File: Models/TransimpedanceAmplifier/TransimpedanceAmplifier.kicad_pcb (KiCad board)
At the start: 2 copper layers, 107 parts, among them J1 Conn_01x02_Socket, J10 Conn_01x02_Pin, J11 Conn_01x24_Socket, J14 Conn_01x24_Socket, J2 Conn_01x02_Socket, J3 Conn_01x03_Pin, J4 Conn_01x02_Pin, J5 Conn_01x02_Pin, J6 Conn_01x02_Pin, J7 Conn_01x02_Pin, J8 Conn_01x02_Pin, J9 Conn_01x02_Pin, Q1 Q_PNP, Q2 Q_NPN, U1 LM7905, -5V, 5%, U10 DAC81401, U11 ISO7641FM, U12 ISO7641FM, U13 ADS8699, U2 LM7805, 5V, 5%, U3 OPA828, U4 AD8615, U5 OP37GPZ, U6 LM7915, -15V, 5%, U7 LM7815, 15V, 5%, U8 LM7805, 5V, 5%, U9 TLV76133, 3.3V, 1%

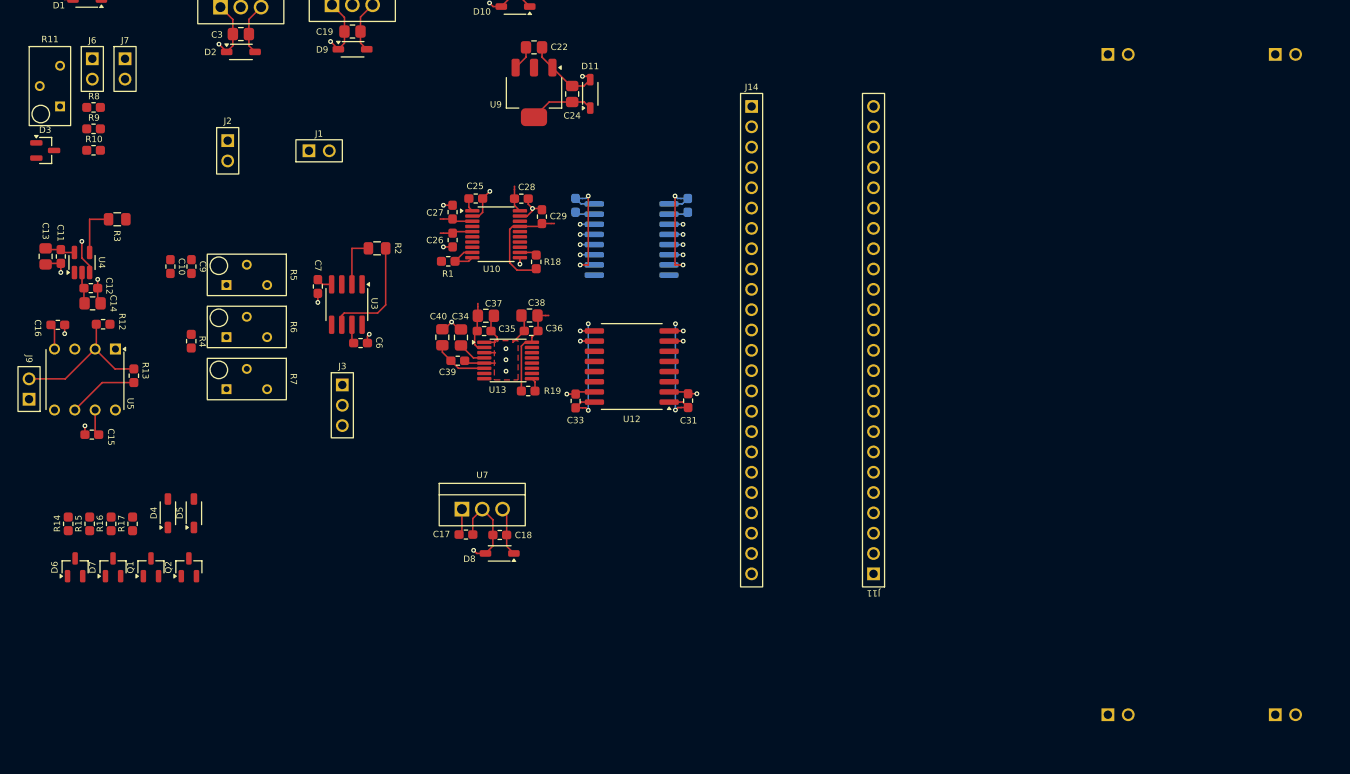
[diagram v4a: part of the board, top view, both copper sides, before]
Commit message: Added notes for power wiring
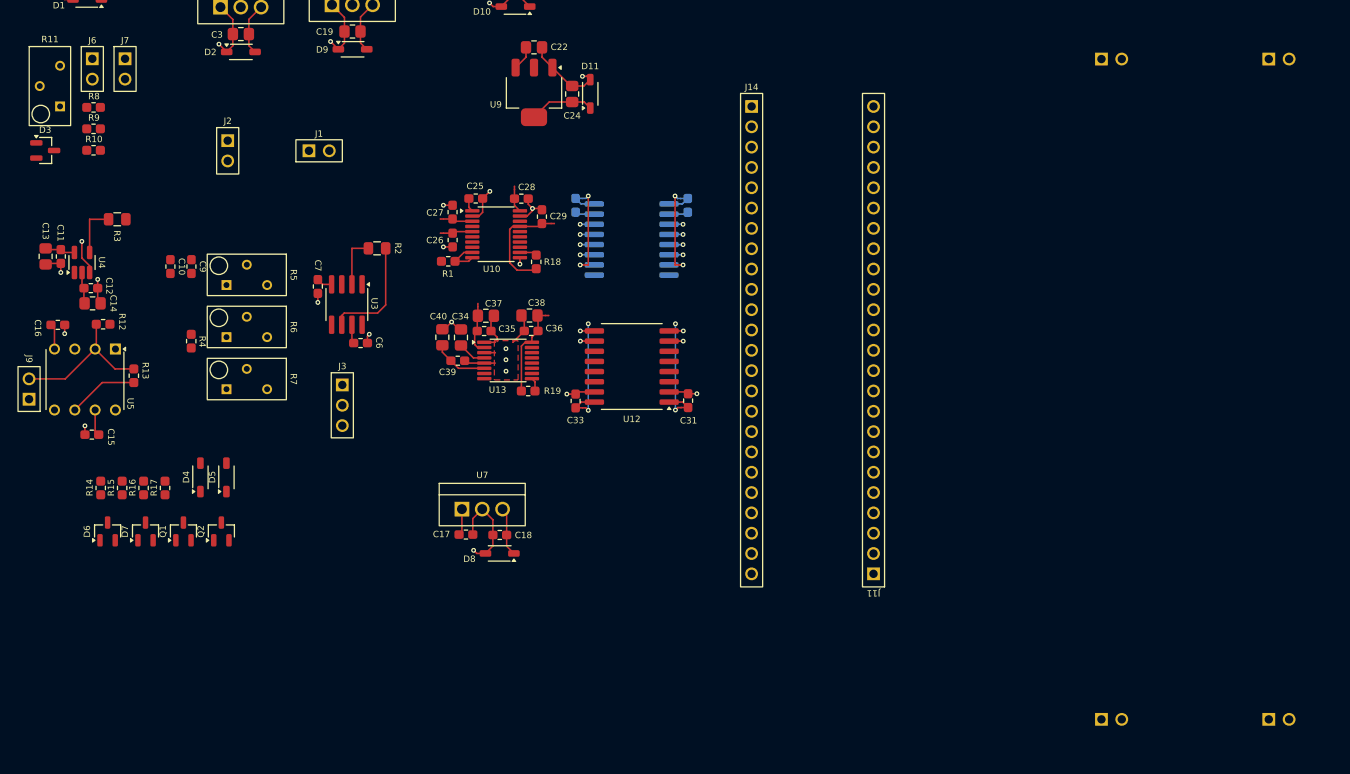
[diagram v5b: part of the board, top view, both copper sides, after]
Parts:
- moved R14 6.05 mm to (87.2, 125.0)
- moved R15 6.05 mm to (89.9, 125.0)
- moved R16 6.05 mm to (92.6, 125.0)
- moved R17 6.05 mm to (95.3, 125.0)
- moved D4 6.05 mm to (99.7, 123.7)
- moved D5 6.05 mm to (102.9, 123.7)
- moved D6 6.05 mm to (88.1, 130.5)
- moved Q1 6.05 mm to (97.6, 130.5)
- moved Q2 6.05 mm to (102.3, 130.5)
- moved D7 6.05 mm to (92.8, 130.5)
- moved BT1 1.00 mm to (224.0, 112.7)
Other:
- board text added: "-1.5 V"
- board text added: "-15 V"
- board text added: "-27 V"
- board text added: "-5 V"
- board text added: "15 V"
- board text added: "18 V"
- board text added: "2.5 V"
- board text added: "27 V"
- board text added: "3.3 V"
- board text added: "5 V"
- board text added: "Bring -15 V all the way around from top of board with long trace on left edge. Topology-wise, from left to right: Conductor connecting two battery terminals -15 V trace (transporting power to bottom) 15 V trace (transporting power to top) Either ordering of -15 V vs. 15 V has an unsavory crossover. Choose the best one after more relevant information is known."
- board text added: "Keep -1.5 V on top of board, route the colliding signal trace under it with vias. This is a much more workable option."
- board text added: "Note: Option to rotate either battery module 180°, reversing the polarity of the exposed battery terminals at each pin socket."
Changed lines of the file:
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@@
 	(footprint "TwoTerminal:SOD-123"
 		(layer "F.Cu")
-		(at 98.87 128.195 90)
+		(at 102.93 123.71 90)
 		(property "Reference" "D5"
 			(at 0.035 -1.77 90)
@@
 	(footprint "TwoTerminal:RESC0603"
 		(layer "F.Cu")
-		(at 88.52 129.5225 90)
+		(at 92.58 125.0375 90)
 		(property "Reference" "R16"
 			(at 0.0475 -1.385 90)
@@
 	(footprint "ThreeTerminal:SOT-23"
 		(layer "F.Cu")
-		(at 88.76 134.9525 90)
+		(at 92.82 130.4675 90)
 		(property "Reference" "D7"
 			(at -0.005 -2.5625 90)
@@
 	(footprint "TwoTerminal:RESC0603"
 		(layer "F.Cu")
-		(at 91.2 129.5225 90)
+		(at 95.26 125.0375 90)
 		(property "Reference" "R17"
 			(at 0.0475 -1.385 90)
@@
 	(footprint "ThreeTerminal:SOT-23"
 		(layer "F.Cu")
-		(at 93.5 134.9525 90)
+		(at 97.56 130.4675 90)
 		(property "Reference" "Q1"
 			(at -0.005 -2.5625 90)
@@
 	(footprint "TwoTerminal:SOD-123"
 		(layer "F.Cu")
-		(at 95.62 128.195 90)
+		(at 99.68 123.71 90)
 		(property "Reference" "D4"
 			(at 0.035 -1.77 90)
@@
 	(footprint "ThreeTerminal:SOT-23"
 		(layer "F.Cu")
-		(at 84.02 134.9525 90)
+		(at 88.08 130.4675 90)
 		(property "Reference" "D6"
 			(at -0.005 -2.5625 90)
@@
 	(footprint "TwoTerminal:RESC0603"
 		(layer "F.Cu")
-		(at 85.84 129.5225 90)
+		(at 89.9 125.0375 90)
 		(property "Reference" "R15"
 			(at 0.0475 -1.385 90)
@@
 	(footprint "TwoTerminal:RESC0603"
 		(layer "F.Cu")
-		(at 83.16 129.5225 90)
+		(at 87.22 125.0375 90)
 		(property "Reference" "R14"
 			(at 0.0475 -1.385 90)
@@
 	(footprint "ThreeTerminal:SOT-23"
 		(layer "F.Cu")
-		(at 98.24 134.9525 90)
+		(at 102.3 130.4675 90)
 		(property "Reference" "Q2"
 			(at -0.005 -2.5625 90)
@@
 	(footprint "Connector_Custom:BatteryModule"
 		(layer "B.Cu")
-		(at 224.85 112.11 -90)
+		(at 224.04 112.69 -90)
 		(property "Reference" "BT1"
 			(at 0.0225 14.7625 90)
@@
 			(polygon
 				(pts
-					(xy 216.635 80.995) (xy 220.365 80.995) (xy 220.365 84.725) (xy 216.635 84.725)
+					(xy 215.825 81.575) (xy 219.555 81.575) (xy 219.555 85.305) (xy 215.825 85.305)
 				)
 			)
@@
 			(polygon
 				(pts
-					(xy 216.635 100.495) (xy 220.365 100.495) (xy 220.365 104.225) (xy 216.635 104.225)
+					(xy 215.825 101.075) (xy 219.555 101.075) (xy 219.555 104.805) (xy 215.825 104.805)
 				)
 			)
@@
 			(polygon
 				(pts
-					(xy 216.635 119.995) (xy 220.365 119.995) (xy 220.365 123.725) (xy 216.635 123.725)
+					(xy 215.825 120.575) (xy 219.555 120.575) (xy 219.555 124.305) (xy 215.825 124.305)
 				)
 			)
@@
 			(polygon
 				(pts
-					(xy 216.635 139.495) (xy 220.365 139.495) (xy 220.365 143.225) (xy 216.635 143.225)
+					(xy 215.825 140.075) (xy 219.555 140.075) (xy 219.555 143.805) (xy 215.825 143.805)
 				)
 			)
@@
 			(polygon
 				(pts
-					(xy 229.335 80.995) (xy 233.065 80.995) (xy 233.065 84.725) (xy 229.335 84.725)
+					(xy 228.525 81.575) (xy 232.255 81.575) (xy 232.255 85.305) (xy 228.525 85.305)
 				)
 			)
@@
 			(polygon
 				(pts
-					(xy 229.335 100.495) (xy 233.065 100.495) (xy 233.065 104.225) (xy 229.335 104.225)
+					(xy 228.525 101.075) (xy 232.255 101.075) (xy 232.255 104.805) (xy 228.525 104.805)
 				)
 			)
@@
 			(polygon
 				(pts
-					(xy 229.335 119.995) (xy 233.065 119.995) (xy 233.065 123.725) (xy 229.335 123.725)
+					(xy 228.525 120.575) (xy 232.255 120.575) (xy 232.255 124.305) (xy 228.525 124.305)
 				)
 			)
@@
 			(polygon
 				(pts
-					(xy 229.335 139.495) (xy 233.065 139.495) (xy 233.065 143.225) (xy 229.335 143.225)
+					(xy 228.525 140.075) (xy 232.255 140.075) (xy 232.255 143.805) (xy 228.525 143.805)
 				)
 			)
@@
 		(layer "Dwgs.User")
 	)
+	(gr_text "2.5 V"
+		(at 80.29 90.41 90)
+		(layer "User.2")
+		(effects
+			(font
+				(size 0.8 0.8)
+				(thickness 0.12)
+			)
+			(justify left bottom)
+		)
+	)
+	(gr_text "Note: Option to rotate either battery module\n180°, reversing the polarity of the exposed\nbattery terminals at each pin socket."
+		(at 209.92 55.17 0)
+		(layer "User.2")
+		(effects
+			(font
+				(size 1.5 1.5)
+				(thickness 0.3)
+				(bold yes)
+			)
+			(justify left top)
+		)
+	)
+	(gr_text "27 V"
+		(at 146.69 138.21 0)
+		(layer "User.2")
+		(effects
+			(font
+				(size 0.8 0.8)
+				(thickness 0.12)
+			)
+			(justify left bottom)
+		)
+	)
+	(gr_text "3.3 V"
+		(at 132.98 71.69 0)
+		(layer "User.2")
+		(effects
+			(font
+				(size 0.8 0.8)
+				(thickness 0.12)
+			)
+			(justify left bottom)
+		)
+	)
+	(gr_text "15 V"
+		(at 124.22 126.16 0)
+		(layer "User.2")
+		(effects
+			(font
+				(size 0.8 0.8)
+				(thickness 0.12)
+			)
+			(justify left bottom)
+		)
+	)
+	(gr_text "Keep -1.5 V on top of board, route the\ncolliding signal trace under it with vias.\nThis is a much more workable option."
+		(at 47.37 95.97 0)
+		(layer "User.2")
+		(effects
+			(font
+				(size 0.8 0.8)
+				(thickness 0.12)
+			)
+			(justify left top)
+		)
+	)
+	(gr_text "-1.5 V"
+		(at 78.51 91.38 90)
+		(layer "User.2")
+		(effects
+			(font
+				(size 0.8 0.8)
+				(thickness 0.12)
+			)
+			(justify left bottom)
+		)
+	)
 	(gr_text "Objective: minimize board size"
 		(at 178.75 168.22 0)
@@
 		)
 	)
+	(gr_text "5 V"
+		(at 90.2 56.89 0)
+		(layer "User.2")
+		(effects
+			(font
+				(size 0.8 0.8)
+				(thickness 0.12)
+			)
+			(justify left bottom)
+		)
+	)
+	(gr_text "-15 V"
+		(at 116.12 57.51 0)
+		(layer "User.2")
+		(effects
+			(font
+				(size 0.8 0.8)
+				(thickness 0.12)
+			)
+			(justify left bottom)
+		)
+	)
+	(gr_text "5 V"
+		(at 130.99 54.15 0)
+		(layer "User.2")
+		(effects
+			(font
+				(size 0.8 0.8)
+				(thickness 0.12)
+			)
+			(justify left bottom)
+		)
+	)
+	(gr_text "18 V"
+		(at 147.04 52.42 0)
+		(layer "User.2")
+		(effects
+			(font
+				(size 0.8 0.8)
+				(thickness 0.12)
+			)
+			(justify left bottom)
+		)
+	)
+	(gr_text "15 V"
+		(at 105.62 127.815 0)
+		(layer "User.2")
+		(effects
+			(font
+				(size 0.8 0.8)
+				(thickness 0.12)
+			)
+			(justify left top)
+		)
+	)
+	(gr_text "-5 V"
+		(at 102.73 57.74 0)
+		(layer "User.2")
+		(effects
+			(font
+				(size 0.8 0.8)
+				(thickness 0.12)
+			)
+			(justify left bottom)
+		)
+	)
+	(gr_text "Bring -15 V all the way around from top\nof board with long trace on left edge.\n\nTopology-wise, from left to right:\nConductor connecting two battery terminals\n-15 V trace (transporting power to bottom)\n15 V trace (transporting power to top)\n\nEither ordering of -15 V vs. 15 V has an\nunsavory crossover. Choose the best one\nafter more relevant information is known."
+		(at 44.95 123.07 0)
+		(layer "User.2")
+		(effects
+			(font
+				(size 0.8 0.8)
+				(thickness 0.12)
+			)
+			(justify left top)
+		)
+	)
+	(gr_text "-15 V"
+		(at 80.81 127.435 0)
+		(layer "User.2")
+		(effects
+			(font
+				(size 0.8 0.8)
+				(thickness 0.12)
+			)
+			(justify left top)
+		)
+	)
+	(gr_text "-27 V"
+		(at 102.48 52.28 0)
+		(layer "User.2")
+		(effects
+			(font
+				(size 0.8 0.8)
+				(thickness 0.12)
+			)
+			(justify left bottom)
+		)
+	)

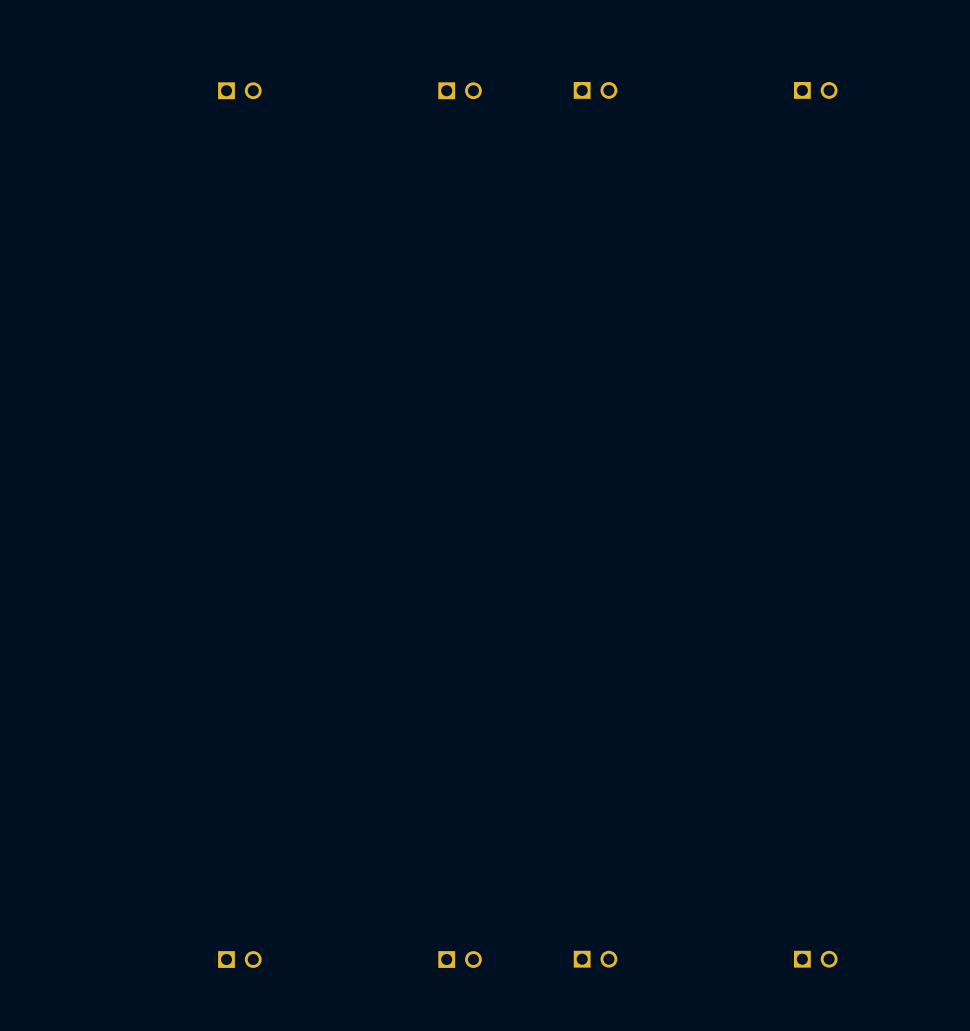
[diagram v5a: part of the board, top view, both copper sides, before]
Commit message: Polarized the battery module by offsetting one of the pin headers
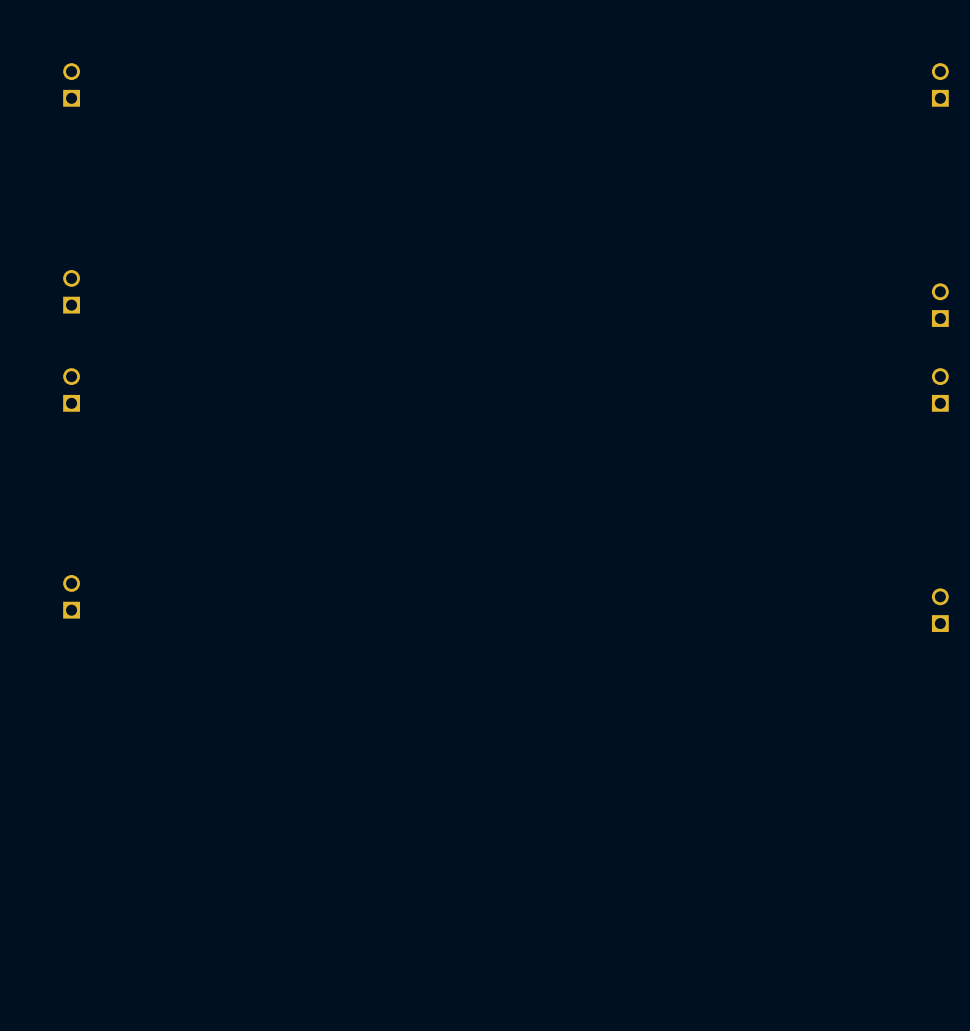
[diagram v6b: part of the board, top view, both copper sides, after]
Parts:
- moved BT1 34.7 mm to (238.9, 81.3), turned to 0 degrees
- moved BT2 19.1 mm to (238.9, 110.3), turned to 0 degrees

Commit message: Rewired the battery modules
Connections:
- BT1 pad 1: Net-(BT1-BT1(+)) -> /Power/Batteries/27V
- BT1 pad 4: GND -> Net-(BT1-BT2(-))
- BT1 pad 5: /Power/Batteries/27V -> /Power/Batteries/18V
- BT1 pad 6: Net-(BT1-BT1(+)) -> Net-(BT1-BT3(-))
- BT1 pad 7: /Power/Batteries/18V -> Net-(BT1-BT3(-))
- BT1 pad 8: Net-(BT1-BT4(-)) -> GND
- BT2 pad 1: GND -> Net-(BT2-BT1(+))
- BT2 pad 4: Net-(BT2-BT2(-)) -> /Power/Batteries/-27V
- BT2 pad 5: Net-(BT1-BT4(-)) -> GND
- BT2 pad 6: GND -> Net-(BT2-BT1(+))
- BT2 pad 7: Net-(BT2-BT2(-)) -> Net-(BT1-BT2(-))
- BT2 pad 8: /Power/Batteries/-27V -> GND
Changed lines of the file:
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@@
 	(net 0 "")
 	(net 1 "Net-(BT1-BT1(-))")
-	(net 2 "Net-(BT1-BT1(+))")
+	(net 2 "Net-(BT1-BT3(-))")
 	(net 3 "/Power/Batteries/18V")
 	(net 4 "/Power/Batteries/27V")
 	(net 5 "GND")
-	(net 6 "Net-(BT1-BT4(-))")
+	(net 6 "Net-(BT1-BT2(-))")
 	(net 7 "/Power/Batteries/-27V")
-	(net 8 "Net-(BT2-BT2(-))")
+	(net 8 "Net-(BT2-BT1(+))")
 	(net 9 "Net-(BT2-BT1(-))")
 	(net 10 "/15V")
@@
 			(layers "*.Cu" "*.Mask")
 			(remove_unused_layers no)
-			(net 5 "GND")
+			(net 8 "Net-(BT2-BT1(+))")
 			(pinfunction "BT1(+)")
 			(pintype "passive")
@@
 			(layers "*.Cu" "*.Mask")
 			(remove_unused_layers no)
-			(net 8 "Net-(BT2-BT2(-))")
+			(net 7 "/Power/Batteries/-27V")
 			(pinfunction "BT2(-)")
 			(pintype "passive")
@@
 			(layers "*.Cu" "*.Mask")
 			(remove_unused_layers no)
-			(net 6 "Net-(BT1-BT4(-))")
+			(net 5 "GND")
 			(pinfunction "BT3(+)")
 			(pintype "passive")
@@
 			(layers "*.Cu" "*.Mask")
 			(remove_unused_layers no)
-			(net 5 "GND")
+			(net 8 "Net-(BT2-BT1(+))")
 			(pinfunction "BT3(-)")
 			(pintype "passive")
@@
 			(layers "*.Cu" "*.Mask")
 			(remove_unused_layers no)
-			(net 8 "Net-(BT2-BT2(-))")
+			(net 6 "Net-(BT1-BT2(-))")
 			(pinfunction "BT4(+)")
 			(pintype "passive")
@@
 			(layers "*.Cu" "*.Mask")
 			(remove_unused_layers no)
-			(net 7 "/Power/Batteries/-27V")
+			(net 5 "GND")
 			(pinfunction "BT4(-)")
 			(pintype "passive")
@@
 			(layers "*.Cu" "*.Mask")
 			(remove_unused_layers no)
-			(net 2 "Net-(BT1-BT1(+))")
+			(net 4 "/Power/Batteries/27V")
 			(pinfunction "BT1(+)")
 			(pintype "passive")
@@
 			(layers "*.Cu" "*.Mask")
 			(remove_unused_layers no)
-			(net 5 "GND")
+			(net 6 "Net-(BT1-BT2(-))")
 			(pinfunction "BT2(-)")
 			(pintype "passive")
@@
 			(layers "*.Cu" "*.Mask")
 			(remove_unused_layers no)
-			(net 4 "/Power/Batteries/27V")
+			(net 3 "/Power/Batteries/18V")
 			(pinfunction "BT3(+)")
 			(pintype "passive")
@@
 			(layers "*.Cu" "*.Mask")
 			(remove_unused_layers no)
-			(net 2 "Net-(BT1-BT1(+))")
+			(net 2 "Net-(BT1-BT3(-))")
 			(pinfunction "BT3(-)")
 			(pintype "passive")
@@
 			(layers "*.Cu" "*.Mask")
 			(remove_unused_layers no)
-			(net 3 "/Power/Batteries/18V")
+			(net 2 "Net-(BT1-BT3(-))")
 			(pinfunction "BT4(+)")
 			(pintype "passive")
@@
 			(layers "*.Cu" "*.Mask")
 			(remove_unused_layers no)
-			(net 6 "Net-(BT1-BT4(-))")
+			(net 5 "GND")
 			(pinfunction "BT4(-)")
 			(pintype "passive")

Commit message: Some more tweaks to prepare for the next round of work on the PCB
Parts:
- moved C10 90.0 mm to (150.9, 26.1)
- moved C9 90.0 mm to (153.5, 26.1)
- moved R4 90.0 mm to (153.5, 35.4)
- moved R5 90.0 mm to (160.4, 27.1)
- moved R7 90.0 mm to (160.4, 40.2)
- moved R6 90.0 mm to (160.4, 33.6)
- moved J6 66.8 mm to (36.5, 28.0)
- moved J7 66.8 mm to (40.6, 28.0)
- moved R10 66.8 mm to (36.7, 38.2)
- moved R11 66.8 mm to (31.2, 30.1)
- moved R8 66.8 mm to (36.7, 32.8)
- moved R9 66.8 mm to (36.7, 35.5)
- moved D3 66.8 mm to (30.7, 38.2)
- moved R14 45.0 mm to (98.0, 168.7)
- moved R15 45.0 mm to (100.7, 168.7)
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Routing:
- net Net-(J9-Pin_2): track 18.8 -> 3.16 mm
- net /TIA_TwoStage/Output: track 8.80 -> 0.00 mm
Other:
- board text removed: "Note: Option to rotate either battery module 180°, reversing the polarity of the exposed battery terminals at each pin socket."
